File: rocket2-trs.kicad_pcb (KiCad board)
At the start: 2 copper layers, 57 x 80 mm, 47 parts, among them J2 SMA, J3 ARM Cortex Debug, U4 AZ1117-3.3, Y1 16MHz

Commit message: trs update 12/14/2025
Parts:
- added U5: LoRA-E5, UCIRP-KiCAD-Lib:LoRa - E5, F.Cu at (193.7, 69.6)
- TP15: value R_DIO5 -> RADIO_DIO5
- TP16: value R_DIO4 -> RADIO_DIO4
- TP17: value R_DIO3 -> RADIO_DIO3
- TP18: value R_DIO2 -> RADIO_DIO2
- TP19: value R_DIO1 -> RADIO_DIO1
- TP20: value R_DIO0 -> RADIO_DIO0
- TP4: value R_nRST -> RADIO_nRST
- TP5: value R_nCS -> RADIO_nCS
- TP6: value R_SCK -> RADIO_SCK
- TP7: value R_MOSI -> RADIO_MOSI
- TP8: value R_MISO -> RADIO_MISO
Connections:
- U1 pad 30: unconnected-(U1-PA9-Pad30) -> UART1 TX
- U1 pad 31: unconnected-(U1-PA10-Pad31) -> UART1 RX
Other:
- board text added: "DIO0"
- board text added: "DIO1"
- board text added: "DIO2"
- board text added: "DIO3"
- board text added: "DIO4"
- board text added: "DIO5"
- board text added: "MISO"
- board text added: "MOSI"
- board text added: "SCK"
- board text added: "nCS"
- board text added: "nRST"

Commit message: TRS fixed
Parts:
- added G***: LOGO, LOGO, F.Cu at (190.8, 54.3)
- moved U5 23.6 mm to (170.4, 66.0)
- moved TP6 16.4 mm to (167.8, 64.1)
- moved TP15 16.3 mm to (167.9, 57.2)
- moved TP7 15.9 mm to (167.8, 66.5)
- moved TP18 15.9 mm to (167.6, 54.0)
- moved TP8 15.9 mm to (167.9, 68.9)
- moved C11 15.8 mm to (176.2, 51.1)
- moved J2 15.8 mm to (184.2, 45.1)
- moved U3 15.8 mm to (177.2, 62.1)
- moved TP4 13.5 mm to (167.9, 59.5)
- moved C6 11.8 mm to (211.6, 65.2)
- moved TP19 11.6 mm to (171.9, 51.6)
- moved U1 11.4 mm to (206.7, 60.5)
- moved C1 11.3 mm to (218.2, 65.2)
- moved C2 11.3 mm to (213.9, 55.6)
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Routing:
- net ETH_nRST: track 38.9 -> 238.9 mm, vias 1 -> 3
- net +3.3V: track 203.8 -> 7.35 mm, vias 7 -> 0
- net ETH_RX: track 41.7 -> 198.5 mm
- net ETH_CP2: track 39.4 -> 190.4 mm
- net ETH_TX: track 45.0 -> 193.4 mm, vias 1 -> 2
- net ETH_CTS: track 61.5 -> 154.4 mm, vias 1 -> 2
- net UART1 TX: track 0.00 -> 72.3 mm
- net UART1 RX: track 0.00 -> 71.0 mm, vias 0 -> 1
- net +5V: track 25.9 -> 72.7 mm, vias 2 -> 0
- net GND: track 15.6 -> 58.8 mm, vias 42 -> 29
- net ETH_RTS: track 50.2 -> 79.3 mm
- net RADIO_DIO3: track 56.1 -> 30.5 mm
- net RADIO_nRST: track 67.1 -> 43.3 mm
- net RADIO_DIO4: track 55.8 -> 33.0 mm
- net RADIO_DIO5: track 77.8 -> 64.0 mm
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- added copper zone on F.Cu, net +3.3V
- removed copper zone on F.Cu, net GND
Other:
- board size 57 x 80 mm -> 72.4 x 80 mm
- board text added: "Telemetry Radio System V.2"
- board text removed: "Telemetry Radio System v1 1/25/2024"

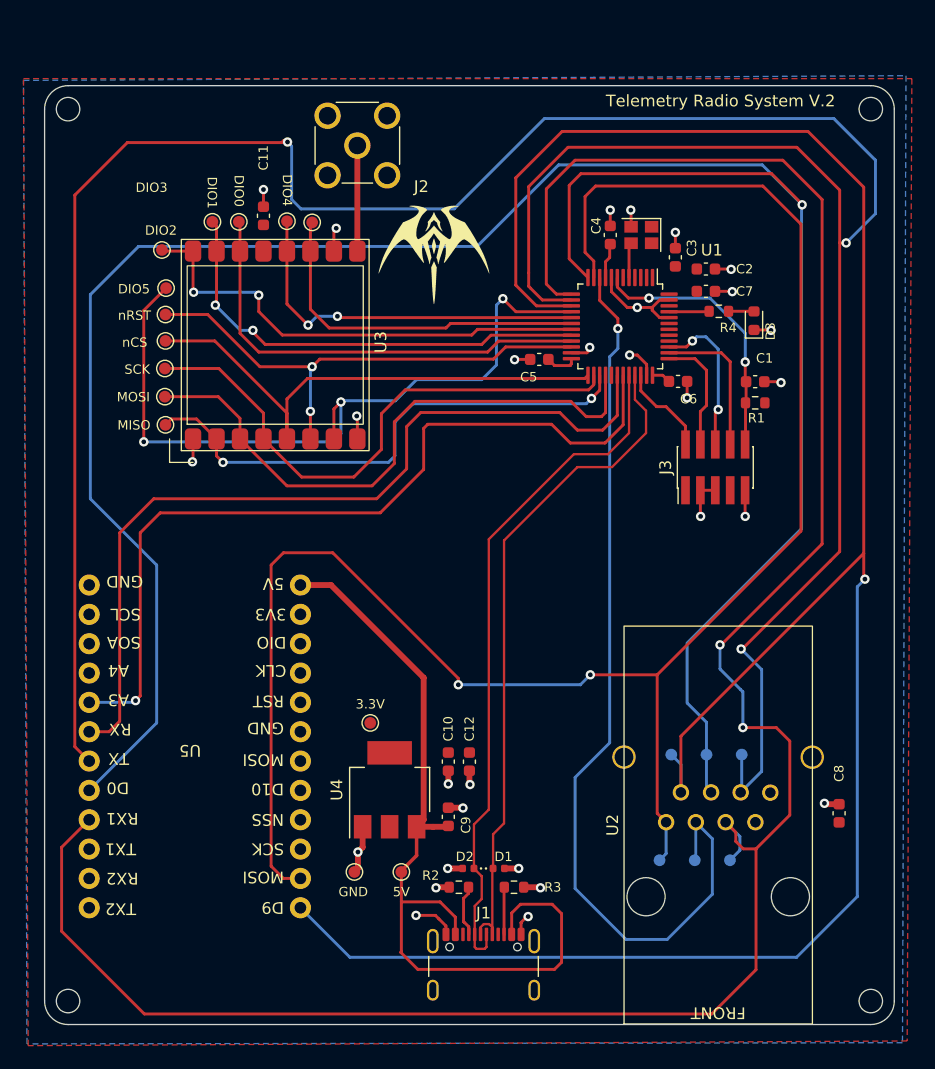
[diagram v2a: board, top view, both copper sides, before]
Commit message: added test points, removed connectors
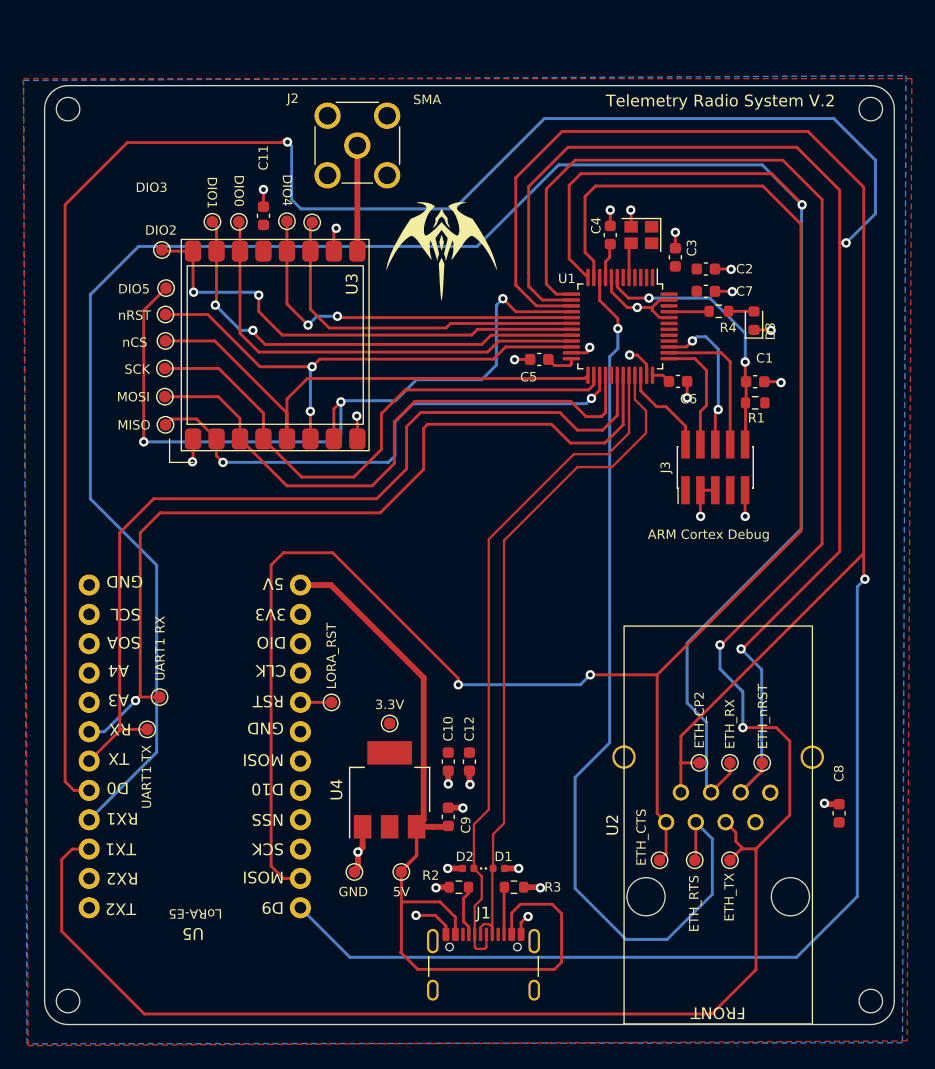
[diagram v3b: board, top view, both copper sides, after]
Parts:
- added TP21: UART1 TX, TestPoint:TestPoint_Pad_D1.0mm, F.Cu at (166.3, 94.8)
- added TP22: UART1 RX, TestPoint:TestPoint_Pad_D1.0mm, F.Cu at (167.4, 92.1)
- added TP23: LORA_RST, TestPoint:TestPoint_Pad_D1.0mm, F.Cu at (182.1, 92.5)
- TP10, TP11, TP12, TP13, TP14, TP9: moved to F.Cu
- moved TP13 2.50 mm to (213.4, 97.7), turned to 0 degrees
- moved TP11 2.12 mm to (216.0, 97.7), turned to 0 degrees
- moved TP9 1.88 mm to (218.8, 97.7), turned to 0 degrees
- moved TP1 1.65 mm to (187.0, 94.3)
- moved G*** 0.72 mm to (191.4, 54.0)
- turned TP10 to 0 degrees
- turned TP12 to 0 degrees
- turned TP14 to 0 degrees
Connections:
- U5 pad 13: unconnected-(U5-SCL_(PB15)-Pad13) -> GND
- U5 pad 17: UART1 RX -> unconnected-(U5-A3_(PB7)-Pad17)
- U5 pad 18: UART1 TX -> UART1 RX
- U5 pad 19: ETH_nRST -> UART1 TX
- U5 pad 20: ETH_RX -> ETH_nRST
- U5 pad 21: ETH_TX -> ETH_RX
- U5 pad 22: unconnected-(U5-TX2_(PA3)-Pad22) -> ETH_TX
- U5 pad 23: (no net) -> unconnected-(U5-RX2_(PA3)-Pad23)
- U5 pad 24: (no net) -> unconnected-(U5-TX2_(PA3)-Pad24)
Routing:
- net ETH_RX: track 198.5 -> 204.2 mm
- net ETH_TX: track 193.4 -> 189.2 mm
- net ETH_nRST: track 238.9 -> 243.0 mm
- net UART1 TX: track 72.3 -> 76.4 mm
- net UART1 RX: track 71.0 -> 74.2 mm
- net LORA_RST: track 0.00 -> 2.65 mm
- net ETH_CP2: track 190.4 -> 188.4 mm

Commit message: added nmos and fixed rx tx
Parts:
- removed TP10: ETH_TX, TestPoint:TestPoint_Pad_D1.0mm
- removed TP11: ETH_RX, TestPoint:TestPoint_Pad_D1.0mm
- removed TP12: ETH_RTS, TestPoint:TestPoint_Pad_D1.0mm
- removed TP13: ETH_CP2, TestPoint:TestPoint_Pad_D1.0mm
- removed TP14: ETH_CTS, TestPoint:TestPoint_Pad_D1.0mm
- removed TP15: RADIO_DIO5, TestPoint:TestPoint_Pad_D1.0mm
- removed TP16: RADIO_DIO4, TestPoint:TestPoint_Pad_D1.0mm
- removed TP17: RADIO_DIO3, TestPoint:TestPoint_Pad_D1.0mm
- removed TP18: RADIO_DIO2, TestPoint:TestPoint_Pad_D1.0mm
- removed TP19: RADIO_DIO1, TestPoint:TestPoint_Pad_D1.0mm
- removed TP20: RADIO_DIO0, TestPoint:TestPoint_Pad_D1.0mm
- removed TP21: UART1 TX, TestPoint:TestPoint_Pad_D1.0mm
- removed TP22: UART1 RX, TestPoint:TestPoint_Pad_D1.0mm
- removed TP9: ETH_nRST, TestPoint:TestPoint_Pad_D1.0mm
- added J4: Conn_01x02_Socket, Connector_PinSocket_1.27mm:PinSocket_1x02_P1.27mm_Vertical, F.Cu at (191.7, 42.5)
- added Q1: NMOS, Package_TO_SOT_SMD:SOT-23, F.Cu at (192.4, 46.5)
- added R5: 100, Resistor_SMD:R_0603_1608Metric, F.Cu at (195.0, 46.4)
- added R6: 100K, Resistor_SMD:R_0603_1608Metric, F.Cu at (196.8, 44.8)
- moved D3 1.33 mm to (218.6, 61.3)
- moved R4 1.33 mm to (215.6, 60.5)
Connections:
- U1 pad 46: unconnected-(U1-PB9-Pad46) -> NMOS
- U5 pad 18: UART1 RX -> UART1 TX
- U5 pad 19: UART1 TX -> UART1 RX
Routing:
- net RADIO_DIO5: track 64.0 -> 30.1 mm, vias 3 -> 2
- net NMOS: track 0.00 -> 31.9 mm, vias 0 -> 2
- net Lowside switch +: track 0.00 -> 9.31 mm
- net ETH_TX: track 189.2 -> 197.3 mm
- net UART1 TX: track 76.4 -> 72.5 mm
- net Lowside switch -: track 0.00 -> 3.68 mm
- net ETH_CTS: track 154.4 -> 150.9 mm
- net Net-(Q1-G): track 0.00 -> 3.45 mm
- net ETH_nRST: track 243.0 -> 239.7 mm
- net ETH_RTS: track 79.3 -> 76.0 mm
- net ETH_RX: track 204.2 -> 201.0 mm
- net RADIO_DIO2: track 40.9 -> 38.2 mm
- net RADIO_DIO1: track 39.4 -> 36.8 mm
- net RADIO_DIO4: track 33.0 -> 30.4 mm
- net RADIO_DIO0: track 38.8 -> 36.3 mm
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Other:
- board text removed: "DIO0"
- board text removed: "DIO1"
- board text removed: "DIO2"
- board text removed: "DIO3"
- board text removed: "DIO4"
- board text removed: "DIO5"

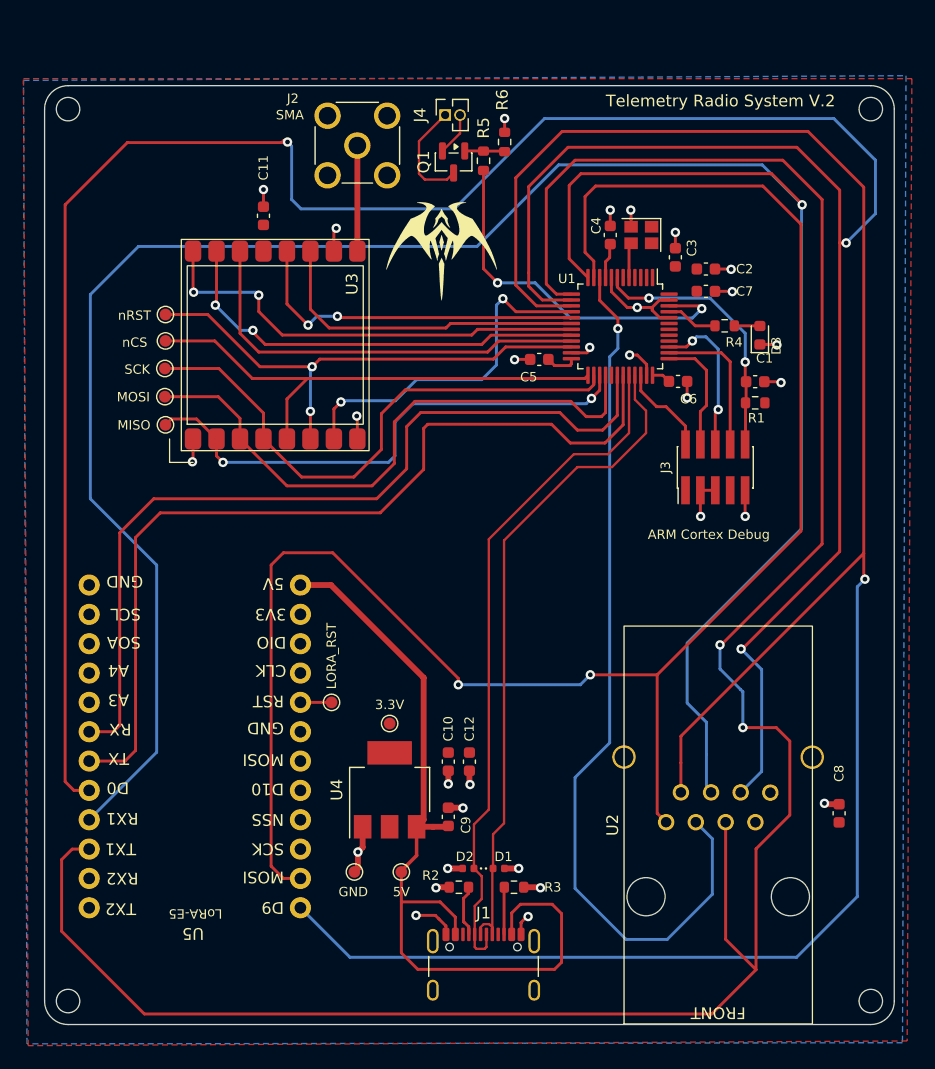
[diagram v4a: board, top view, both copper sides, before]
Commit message: Fixed board size and removed eth from lora
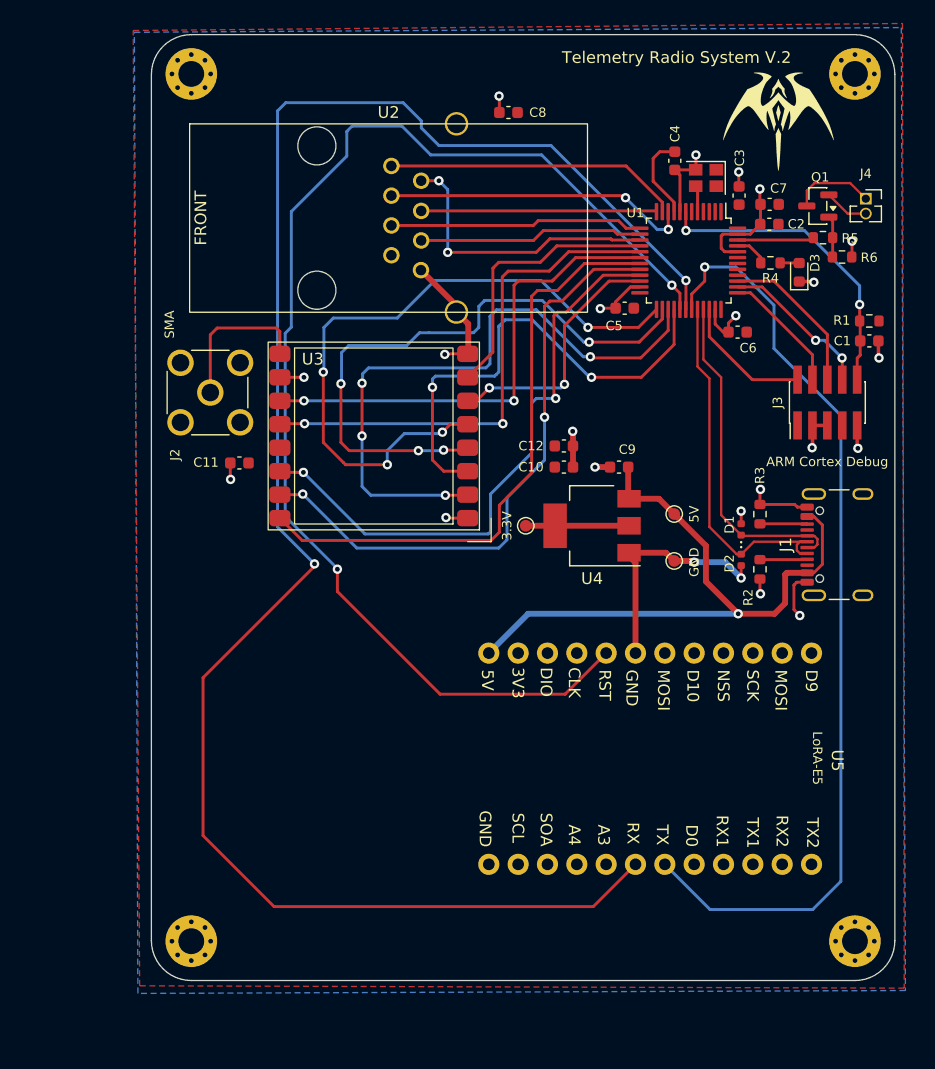
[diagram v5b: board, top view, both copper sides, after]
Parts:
- removed TP23: LORA_RST, TestPoint:TestPoint_Pad_D1.0mm
- removed TP4: RADIO_nRST, TestPoint:TestPoint_Pad_D1.0mm
- removed TP5: RADIO_nCS, TestPoint:TestPoint_Pad_D1.0mm
- removed TP6: RADIO_SCK, TestPoint:TestPoint_Pad_D1.0mm
- removed TP7: RADIO_MOSI, TestPoint:TestPoint_Pad_D1.0mm
- removed TP8: RADIO_MISO, TestPoint:TestPoint_Pad_D1.0mm
- added REF**: MountingHole_2.2mm_M2_Pad_Via, MountingHole:MountingHole_2.2mm_M2_Pad_Via, F.Cu at (170.1, 112.9)
- added REF**: MountingHole_2.2mm_M2_Pad_Via, MountingHole:MountingHole_2.2mm_M2_Pad_Via, F.Cu at (170.1, 39.0)
- added REF**: MountingHole_2.2mm_M2_Pad_Via, MountingHole:MountingHole_2.2mm_M2_Pad_Via, F.Cu at (226.7, 112.9)
- added REF**: MountingHole_2.2mm_M2_Pad_Via, MountingHole:MountingHole_2.2mm_M2_Pad_Via, F.Cu at (226.7, 39.0)
- moved C8 66.0 mm to (197.1, 42.3), turned to 180 degrees
- moved U2 58.9 mm to (186.9, 51.3), turned to 0 degrees
- moved J1 48.4 mm to (226.3, 79.1), turned to 90 degrees
- moved TP3 38.4 mm to (211.2, 76.5), turned to 90 degrees
- moved R3 38.1 mm to (218.6, 76.5), turned to 90 degrees
- moved TP2 38.0 mm to (211.2, 80.5), turned to 90 degrees
- moved R2 37.3 mm to (218.6, 81.2), turned to -90 degrees
- moved J4 36.5 mm to (227.6, 49.6), turned to 0 degrees
- moved D1 35.5 mm to (217.0, 77.8), turned to 90 degrees
- moved D2 35.1 mm to (217.0, 80.4), turned to -90 degrees
- moved C9 33.2 mm to (206.6, 72.5), turned to 180 degrees
- moved U5 32.4 mm to (178.9, 97.3), turned to -90 degrees
- moved Q1 31.3 mm to (223.5, 50.2), turned to 180 degrees
- moved G*** 30.8 mm to (220.1, 43.0)
- moved R6 30.4 mm to (225.6, 54.6), turned to 0 degrees
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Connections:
- U1 pad 29: unconnected-(U1-PA8-Pad29) -> LORA_RST
- U5 pad 11: ETH_CTS -> unconnected-(U5-DI0_(PB10)-Pad11)
- U5 pad 12: ETH_CP2 -> unconnected-(U5-D9_(PA9)-Pad12)
- U5 pad 20: ETH_nRST -> unconnected-(U5-D0_(PA0)-Pad20)
- U5 pad 21: ETH_RX -> unconnected-(U5-RX1_(PC0)-Pad21)
- U5 pad 22: ETH_TX -> unconnected-(U5-TX1_(PC1)-Pad22)
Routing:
- net ETH_nRST: track 239.7 -> 19.1 mm, vias 3 -> 0
- net ETH_RX: track 201.0 -> 20.1 mm, vias 1 -> 0
- net ETH_TX: track 197.3 -> 21.6 mm, vias 2 -> 0
- net ETH_CP2: track 186.8 -> 24.9 mm, vias 1 -> 2
- net ETH_CTS: track 150.9 -> 25.2 mm, vias 2 -> 0
- net LORA_RST: track 2.65 -> 107.0 mm, vias 0 -> 2
- net UART1 TX: track 72.5 -> 152.0 mm, vias 0 -> 2
- net ETH_RTS: track 76.0 -> 26.3 mm, vias 1 -> 2
- net GND: track 60.0 -> 90.0 mm, vias 30 -> 23
- net USB_D+: track 57.6 -> 28.7 mm
- net USB_D-: track 58.7 -> 31.1 mm
- net NMOS: track 31.9 -> 6.53 mm, vias 2 -> 0
- net RADIO_nRST: track 43.3 -> 21.8 mm
- net +5V: track 72.7 -> 55.9 mm, vias 0 -> 1
- net RADIO_DIO1: track 36.8 -> 52.2 mm
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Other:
- board size 72.4 x 80 mm -> 63.4 x 80.6 mm
- board text removed: "MISO"
- board text removed: "MOSI"
- board text removed: "SCK"
- board text removed: "nCS"
- board text removed: "nRST"
